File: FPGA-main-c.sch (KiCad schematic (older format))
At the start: 26 parts, among them IC1 IS25LP256D-JLLE, J1 jtag_header_01x06, SW1 SW_Push, U1 XC7A75T-FTG256

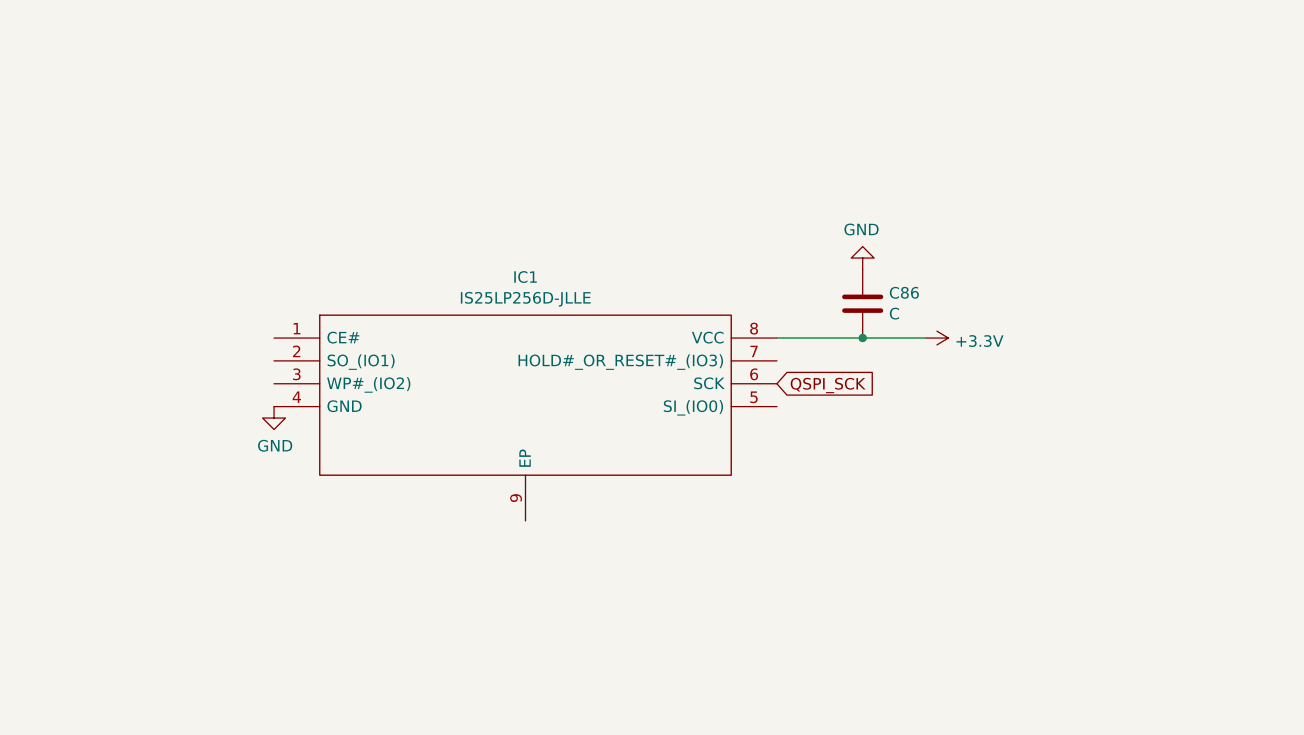
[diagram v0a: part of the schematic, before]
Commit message: Add wire up for Q-SPI flash module.
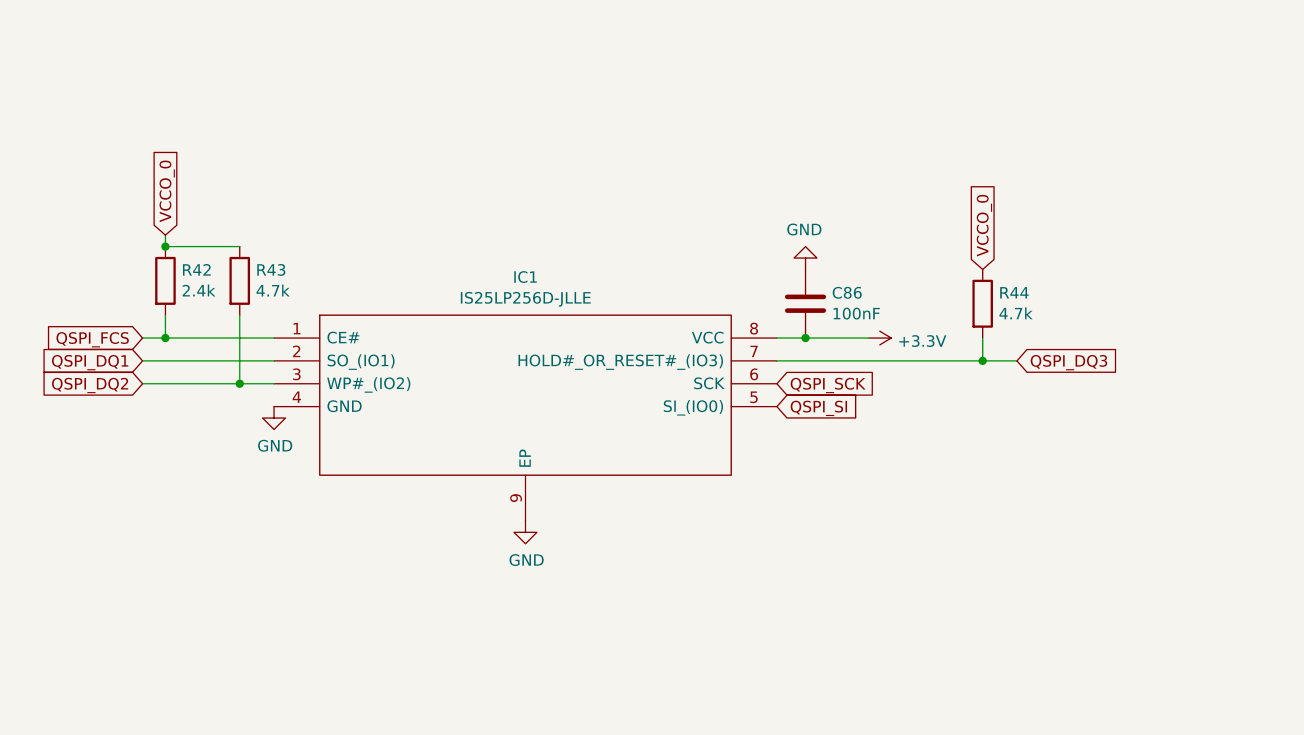
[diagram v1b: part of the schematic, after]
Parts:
- added R42: 2.4k, Resistor_SMD:R_0603_1608Metric, symbol Device:R
- added R43, R44: 4.7k, Resistor_SMD:R_0603_1608Metric, symbol Device:R
- C86: value C -> 100nF; footprint (none) -> Capacitor_SMD:C_0603_1608Metric
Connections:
- net GND: now also IC1.9 (EP)
- net VCCO_0: now also R42.1, R43.1, R44.1
- net QSPI_FCS: now reaches IC1.1 (CE#)
- net QSPI_FCS: now also R42.2
- net QSPI_DQ1: now reaches IC1.2 (SO_(IO1))
- net QSPI_DQ2: now reaches IC1.3 (WP#_(IO2))
- net QSPI_DQ2: now also R43.2
- net QSPI_SI: now reaches IC1.5 (SI_(IO0))
- net QSPI_DQ3: now reaches IC1.7 (HOLD#_OR_RESET#_(IO3))
- net QSPI_DQ3: now also R44.2
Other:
- moved on the sheet: C86
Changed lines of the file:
@@
 L Device:C C86
 U 1 1 60FE861B
-P 5000 1725
-F 0 "C86" H 5115 1771 50  0000 L CNN
-F 1 "C" H 5115 1680 50  0000 L CNN
-F 2 "" H 5038 1575 50  0001 C CNN
-F 3 "~" H 5000 1725 50  0001 C CNN
-	1    5000 1725
+P 4750 1725
+F 0 "C86" H 4865 1771 50  0000 L CNN
+F 1 "100nF" H 4865 1680 50  0000 L CNN
+F 2 "Capacitor_SMD:C_0603_1608Metric" H 4788 1575 50  0001 C CNN
+F 3 "~" H 4750 1725 50  0001 C CNN
+	1    4750 1725
 	1    0    0    -1
 $EndComp
@@
 L power:GND #PWR0177
 U 1 1 60FE8B3C
-P 5000 1575
-F 0 "#PWR0177" H 5000 1325 50  0001 C CNN
-F 1 "GND" H 5005 1402 50  0000 C CNN
-F 2 "" H 5000 1575 50  0001 C CNN
-F 3 "" H 5000 1575 50  0001 C CNN
-	1    5000 1575
+P 4750 1575
+F 0 "#PWR0177" H 4750 1325 50  0001 C CNN
+F 1 "GND" H 4755 1402 50  0000 C CNN
+F 2 "" H 4750 1575 50  0001 C CNN
+F 3 "" H 4750 1575 50  0001 C CNN
+	1    4750 1575
 	-1   0    0    1
 $EndComp
-Wire Wire Line
-	4625 1875 5000 1875
-Connection ~ 5000 1875
-Wire Wire Line
-	5000 1875 5275 1875
+Connection ~ 4750 1875
+Wire Wire Line
+	4750 1875 5025 1875
 $Comp
 L power:+3.3V #PWR0178
 U 1 1 60FEA10A
-P 5275 1875
-F 0 "#PWR0178" H 5275 1725 50  0001 C CNN
-F 1 "+3.3V" V 5290 2003 50  0000 L CNN
-F 2 "" H 5275 1875 50  0001 C CNN
-F 3 "" H 5275 1875 50  0001 C CNN
-	1    5275 1875
+P 5025 1875
+F 0 "#PWR0178" H 5025 1725 50  0001 C CNN
+F 1 "+3.3V" V 5040 2003 50  0000 L CNN
+F 2 "" H 5025 1875 50  0001 C CNN
+F 3 "" H 5025 1875 50  0001 C CNN
+	1    5025 1875
 	0    1    1    0
 $EndComp
-Text GLabel 4625 2075 2    50   Input ~ 0
-QSPI_SCK
 Text GLabel 14975 8025 0    50   Input ~ 0
 PROGRAM_B_0
@@
 Text GLabel 9475 4425 0    50   Input ~ 0
 VCCO_0
+$Comp
+L power:GND #PWR0169
+U 1 1 60BEFDBC
+P 3525 2675
+F 0 "#PWR0169" H 3525 2425 50  0001 C CNN
+F 1 "GND" H 3530 2502 50  0000 C CNN
+F 2 "" H 3525 2675 50  0001 C CNN
+F 3 "" H 3525 2675 50  0001 C CNN
+	1    3525 2675
+	1    0    0    -1
+$EndComp
+Wire Wire Line
+	4625 1875 4750 1875
+Text GLabel 1850 1875 0    50   Input ~ 0
+QSPI_FCS
+Text GLabel 1850 1975 0    50   Input ~ 0
+QSPI_DQ1
+Text GLabel 1850 2075 0    50   Input ~ 0
+QSPI_DQ2
+Text GLabel 5675 1975 2    50   Input ~ 0
+QSPI_DQ3
+Text GLabel 4625 2175 2    50   Input ~ 0
+QSPI_SI
+Text GLabel 4625 2075 2    50   Input ~ 0
+QSPI_SCK
+$Comp
+L Device:R R42
+U 1 1 60C3D285
+P 1950 1625
+F 0 "R42" H 2020 1671 50  0000 L CNN
+F 1 "2.4k" H 2020 1580 50  0000 L CNN
+F 2 "Resistor_SMD:R_0603_1608Metric" V 1880 1625 50  0001 C CNN
+F 3 "~" H 1950 1625 50  0001 C CNN
+	1    1950 1625
+	1    0    0    -1
+$EndComp
+Wire Wire Line
+	1950 1775 1950 1875
+$Comp
+L Device:R R43
+U 1 1 60C407A0
+P 2275 1625
+F 0 "R43" H 2345 1671 50  0000 L CNN
+F 1 "4.7k" H 2345 1580 50  0000 L CNN
+F 2 "Resistor_SMD:R_0603_1608Metric" V 2205 1625 50  0001 C CNN
+F 3 "~" H 2275 1625 50  0001 C CNN
+	1    2275 1625
+	1    0    0    -1
+$EndComp
+Wire Wire Line
+	2275 1775 2275 2075
+Wire Wire Line
+	1850 1975 2425 1975
+Connection ~ 1950 1875
+Wire Wire Line
+	1950 1875 1850 1875
+Connection ~ 2275 2075
+Wire Wire Line
+	2275 2075 1850 2075
+Wire Wire Line
+	1950 1875 2425 1875
+Wire Wire Line
+	2275 2075 2425 2075
+Text GLabel 1950 1425 1    50   Input ~ 0
+VCCO_0
+Wire Wire Line
+	2275 1475 1950 1475
+Wire Wire Line
+	1950 1425 1950 1475
+Connection ~ 1950 1475
+Wire Wire Line
+	5675 1975 5525 1975
+Text GLabel 5525 1575 1    50   Input ~ 0
+VCCO_0
+$Comp
+L Device:R R44
+U 1 1 60C6B871
+P 5525 1725
+F 0 "R44" H 5595 1771 50  0000 L CNN
+F 1 "4.7k" H 5595 1680 50  0000 L CNN
+F 2 "Resistor_SMD:R_0603_1608Metric" V 5455 1725 50  0001 C CNN
+F 3 "~" H 5525 1725 50  0001 C CNN
+	1    5525 1725
+	1    0    0    -1
+$EndComp
+Wire Wire Line
+	5525 1875 5525 1975
+Connection ~ 5525 1975
+Wire Wire Line
+	5525 1975 4625 1975
 $EndSCHEMATC
